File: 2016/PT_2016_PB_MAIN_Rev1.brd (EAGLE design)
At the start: 151.1 x 202.8 mm, 113 parts, among them Q1 Q_IRFS7437PbF, Q11 Q_IRFS7437PbF, Q12 2N7002, Q14 Q_IRFS7437PbF, Q16 Q_IRFS7437PbF, Q20 Q_IRFS7437PbF, Q6 Q_IRFS7437PbF, Q7 Q_IRFS7437PbF, Q9 Q_IRFS7437PbF

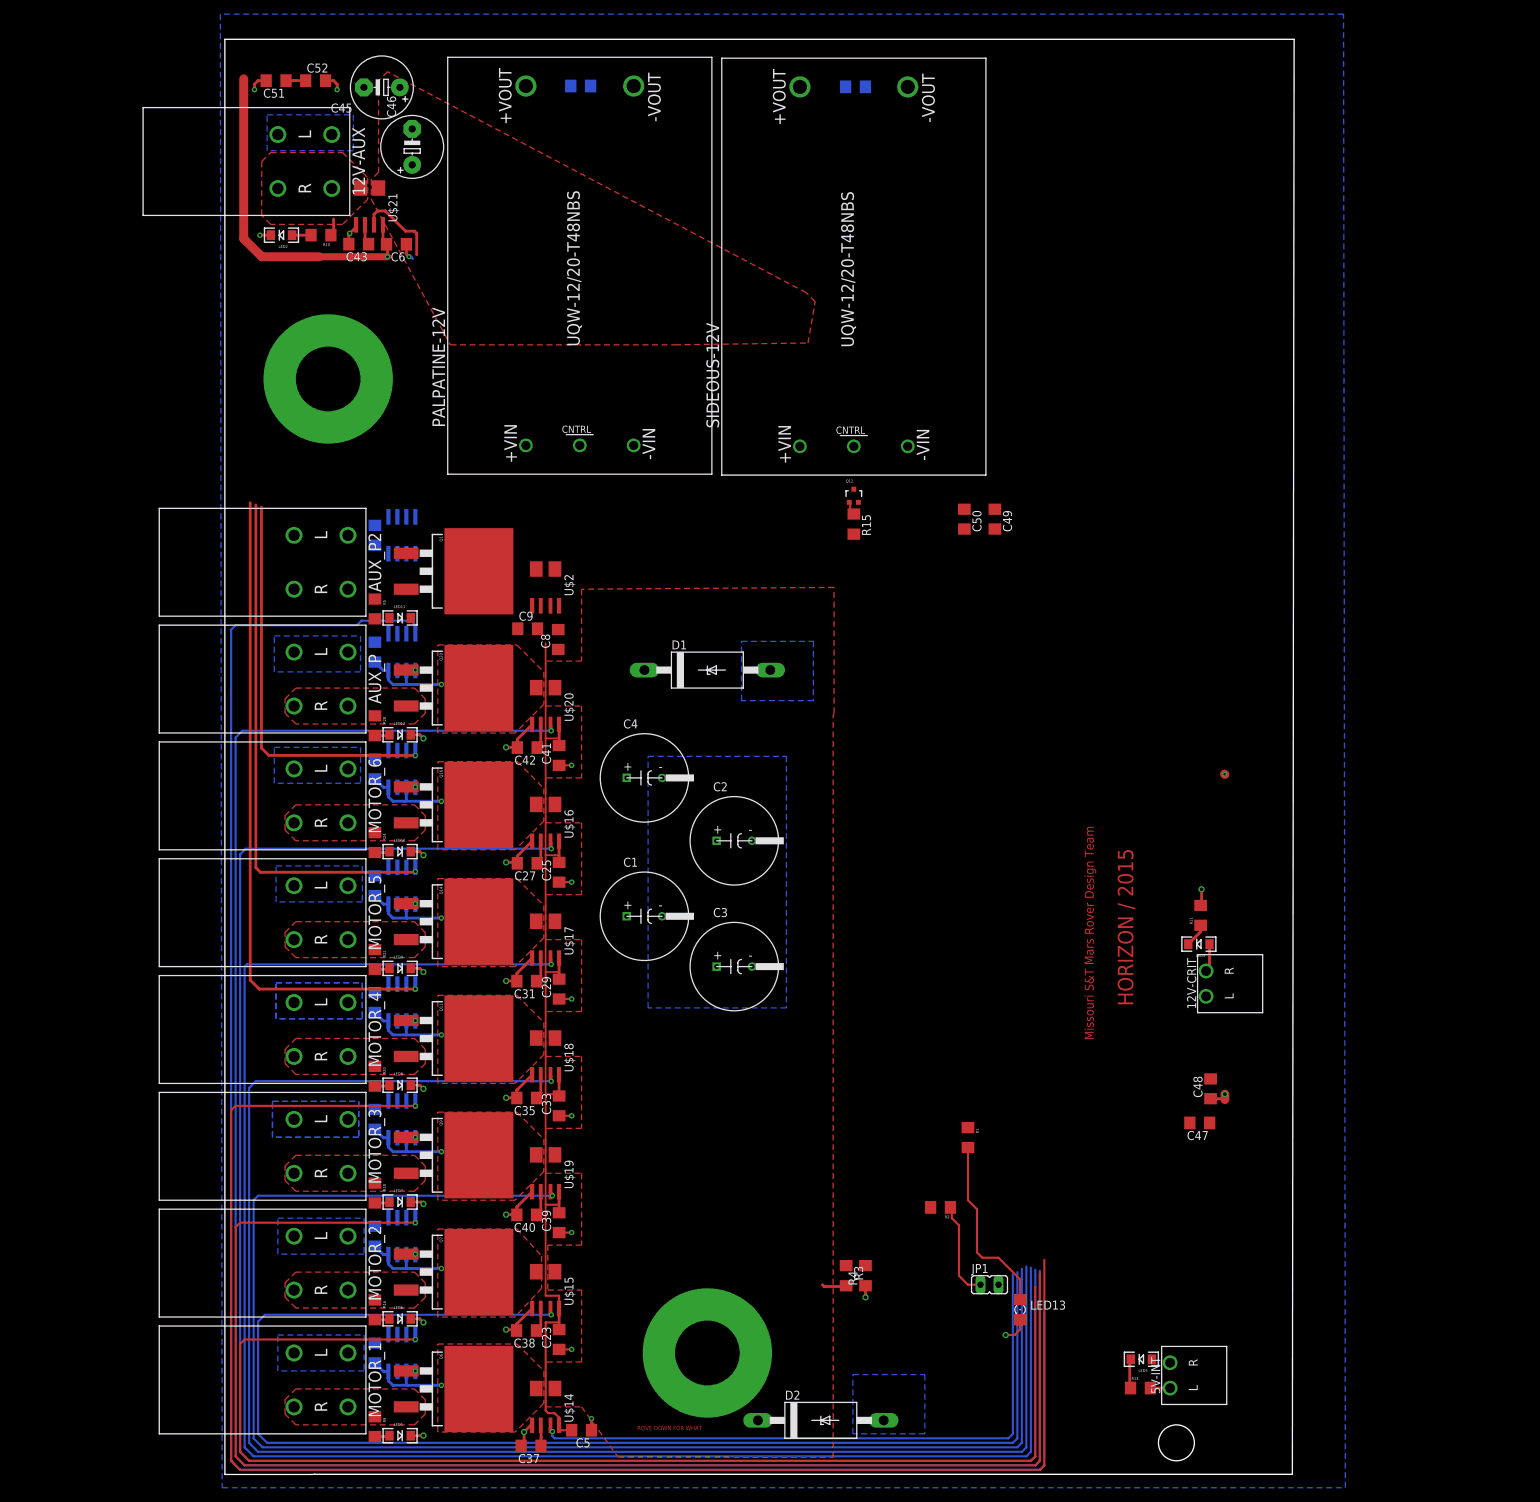
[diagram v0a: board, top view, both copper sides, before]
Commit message: Added Murata 5V Converter and TI uC
Rearranged board
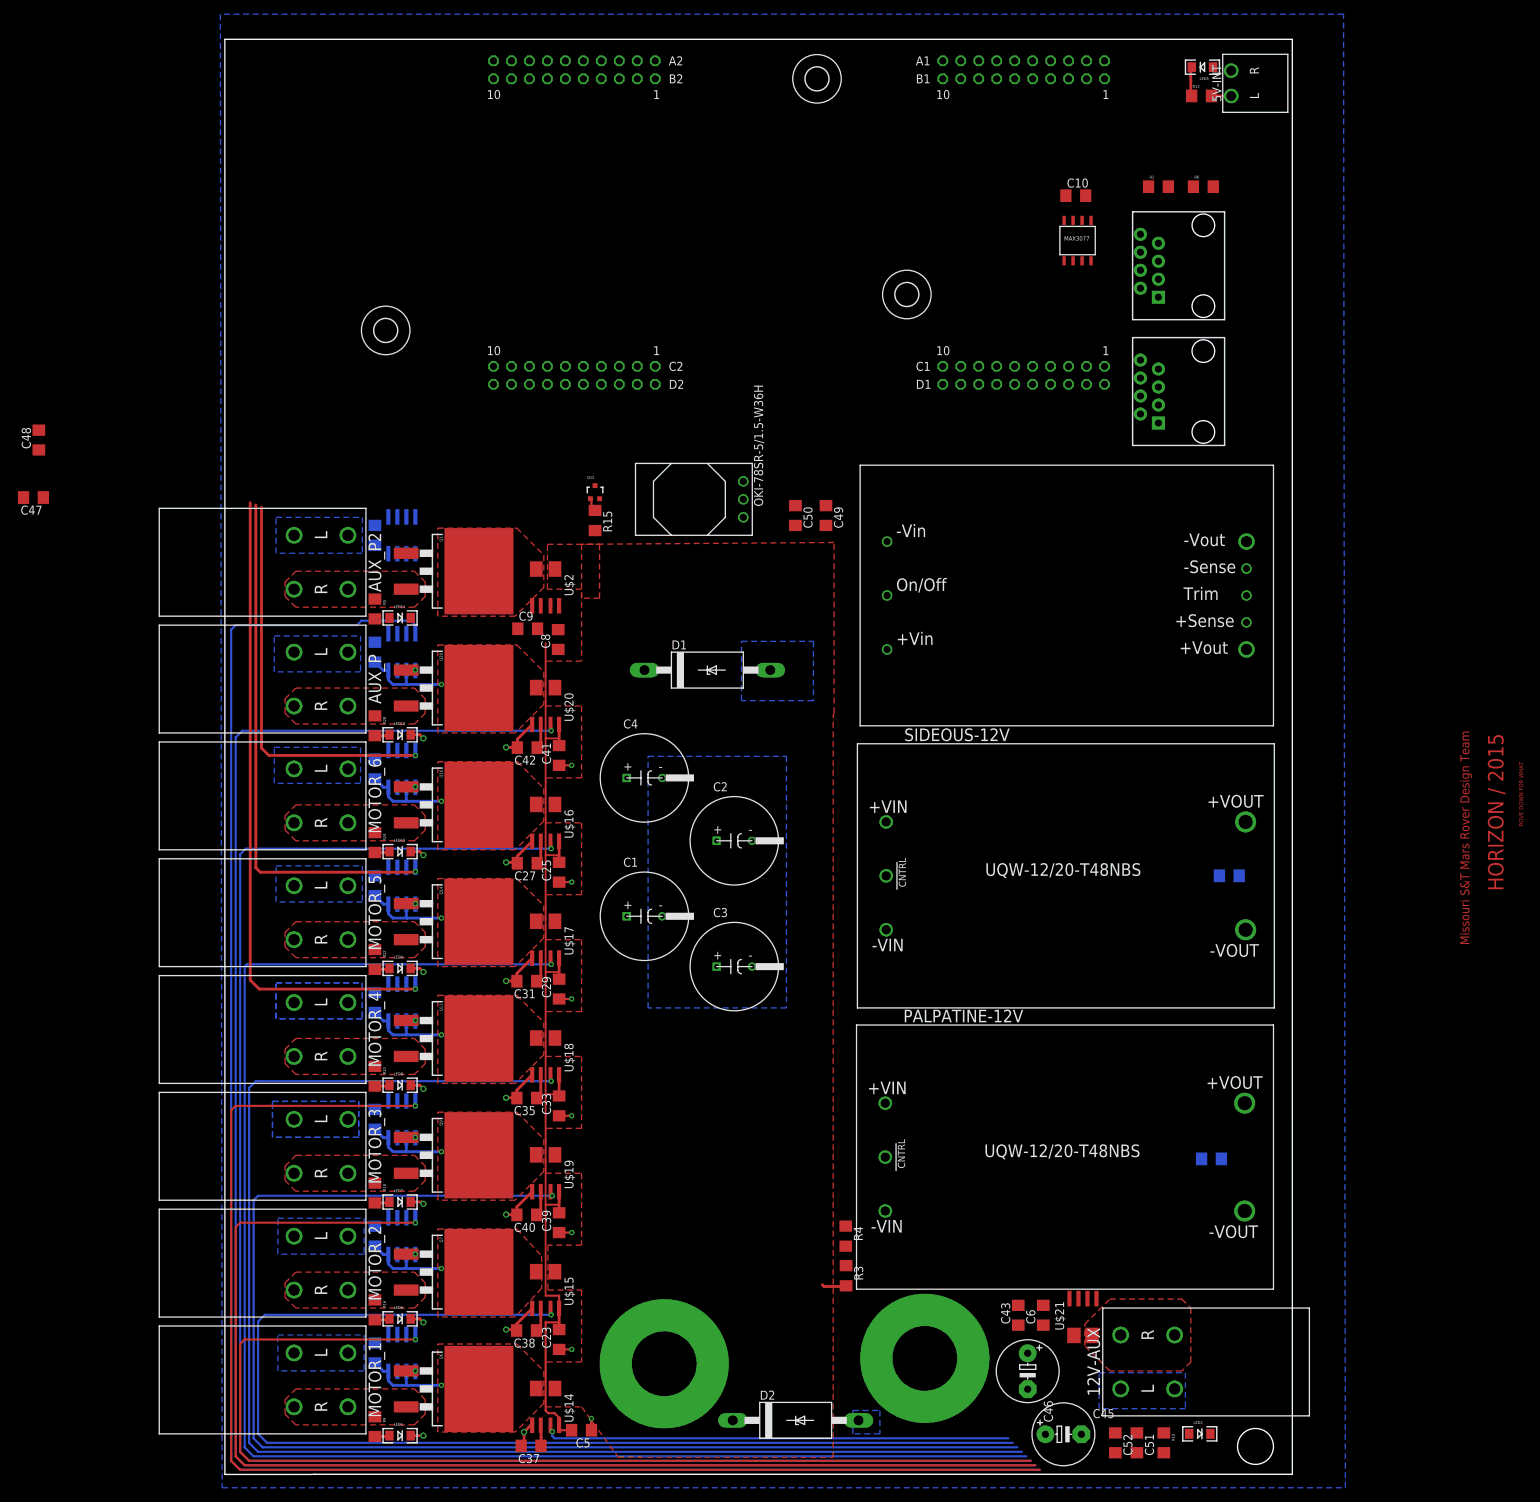
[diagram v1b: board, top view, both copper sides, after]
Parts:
- removed 12V-CRIT: H_WR-TBL_321*0002HORIZ, MRDT-2015-PowerBoard:691322110002
- removed JP1: (no value), jumper:JP1
- removed LED13: (no value), SparkFun-LED:FKIT-LED-1206
- removed LED3: (no value), SparkFun-LED:LED-1206
- removed R11: 1kΩ, SparkFun-Passives:1206
- removed R2: 10k Ohm, SparkFun-Passives:1206
- added C10: 1uF, resistor:C1206
- added OKI-78SR-5/1.5-W36H: Q_OKI-78SR, MRDT-2015-PowerBoard:OKI-78SRH
- added R6: 120 Ohm, SparkFun-Passives:1206
- added U$12: MAX3077, MAX3077:MAX3070E
- added U$23, U$5: RJ45-8PTH, SparkFun-Connectors:RJ45-8
- added U$3: MURATA_5V_DC-DC_CONVERTER, Murata_5V_DC-DC_Converter:MURATA_5V_DC-DC_CONVERTER
- added U$4: TIVA-C-CONNECTED, MRDT-2015-General:TIVA-C-CONNECTED
- R1: value 1k Ohm -> 120 Ohm
- moved C51 227.8 mm to (124.2, 0.00), turned to 270 degrees
- moved C52 223.3 mm to (121.2, 0.00), turned to 270 degrees
- moved LED2 213.4 mm to (133.1, 1.27), turned to 0 degrees
- moved C45 213.4 mm to (113.8, 1.21), turned to 0 degrees
- moved R10 208.1 mm to (128.0, 0.00), turned to 270 degrees
- moved 12V-AUX 207.3 mm to (125.7, 11.4), turned to 90 degrees
- moved C46 193.7 mm to (108.8, 10.1), turned to 270 degrees
- moved C48 189.3 mm to (-31.0, 141.7)
- moved C47 187.0 mm to (-31.8, 133.6)
- moved U$21 186.6 mm to (116.6, 17.8), turned to 0 degrees
- moved 5V-INT 182.8 mm to (137.5, 192.2)
- moved LED5 182.8 mm to (133.5, 194.4)
- moved R13 182.8 mm to (133.3, 190.4)
- moved C43 177.8 mm to (107.4, 18.0), turned to 90 degrees
- moved C6 176.8 mm to (111.0, 18.0), turned to 90 degrees
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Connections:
- removed net 12V-CRIT: 12V-CRIT.R, LED3.A
- removed net INFO_LED: R1.1
- removed net JUMPER_SIG_IN: JP1.1, R2.1
- removed net N$11: LED13.A, R1.2
- new net N$18: R6.1, U$12.Z, U$5.2
- new net N$19: R1.2, U$12.B, U$5.6
- new net N$20: R1.1, U$12.A, U$5.3
- new net N$21: U$12.DI
- new net RXD: U$12.RO
- net +5V: now also C10.1, U$12.VCC; no longer R2.2
- net GND: now also C10.2, U$12.GND, U$5.7, U$5.8; no longer 12V-CRIT.L, JP1.2, LED13.C, R11.2
- net N$3: now also R6.2, U$12.Y, U$5.1; no longer LED3.C, R11.1
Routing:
- net +5V: track 207.1 -> 150.6 mm, vias 3 -> 0
- net M3-SIG: track 221.3 -> 191.3 mm
- net AUX_P-IMEAS: track 288.8 -> 261.1 mm
- net M2-SIG: track 199.7 -> 172.3 mm
- net M6-IMEAS: track 270.3 -> 243.0 mm
- net M5-IMEAS: track 250.3 -> 223.4 mm
- net M4-IMEAS: track 230.4 -> 203.9 mm
- net N$11: track 25.9 -> 0.00 mm
- net M3-IMEAS: track 210.8 -> 185.3 mm
- net M1-SIG: track 178.1 -> 153.3 mm
- net M2-IMEAS: track 190.3 -> 165.9 mm
- net M1-IMEAS: track 89.7 -> 66.2 mm
- net AUX_P-SIG: track 282.8 -> 260.3 mm
- net GND: track 86.8 -> 66.6 mm, vias 29 -> 21
- net JUMPER_SIG_IN: track 13.7 -> 0.00 mm
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- removed copper zone on layer 1, net N$7
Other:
- board size 151.1 x 202.8 mm -> 150.9 x 202.8 mm

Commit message: Added final components and started routing.
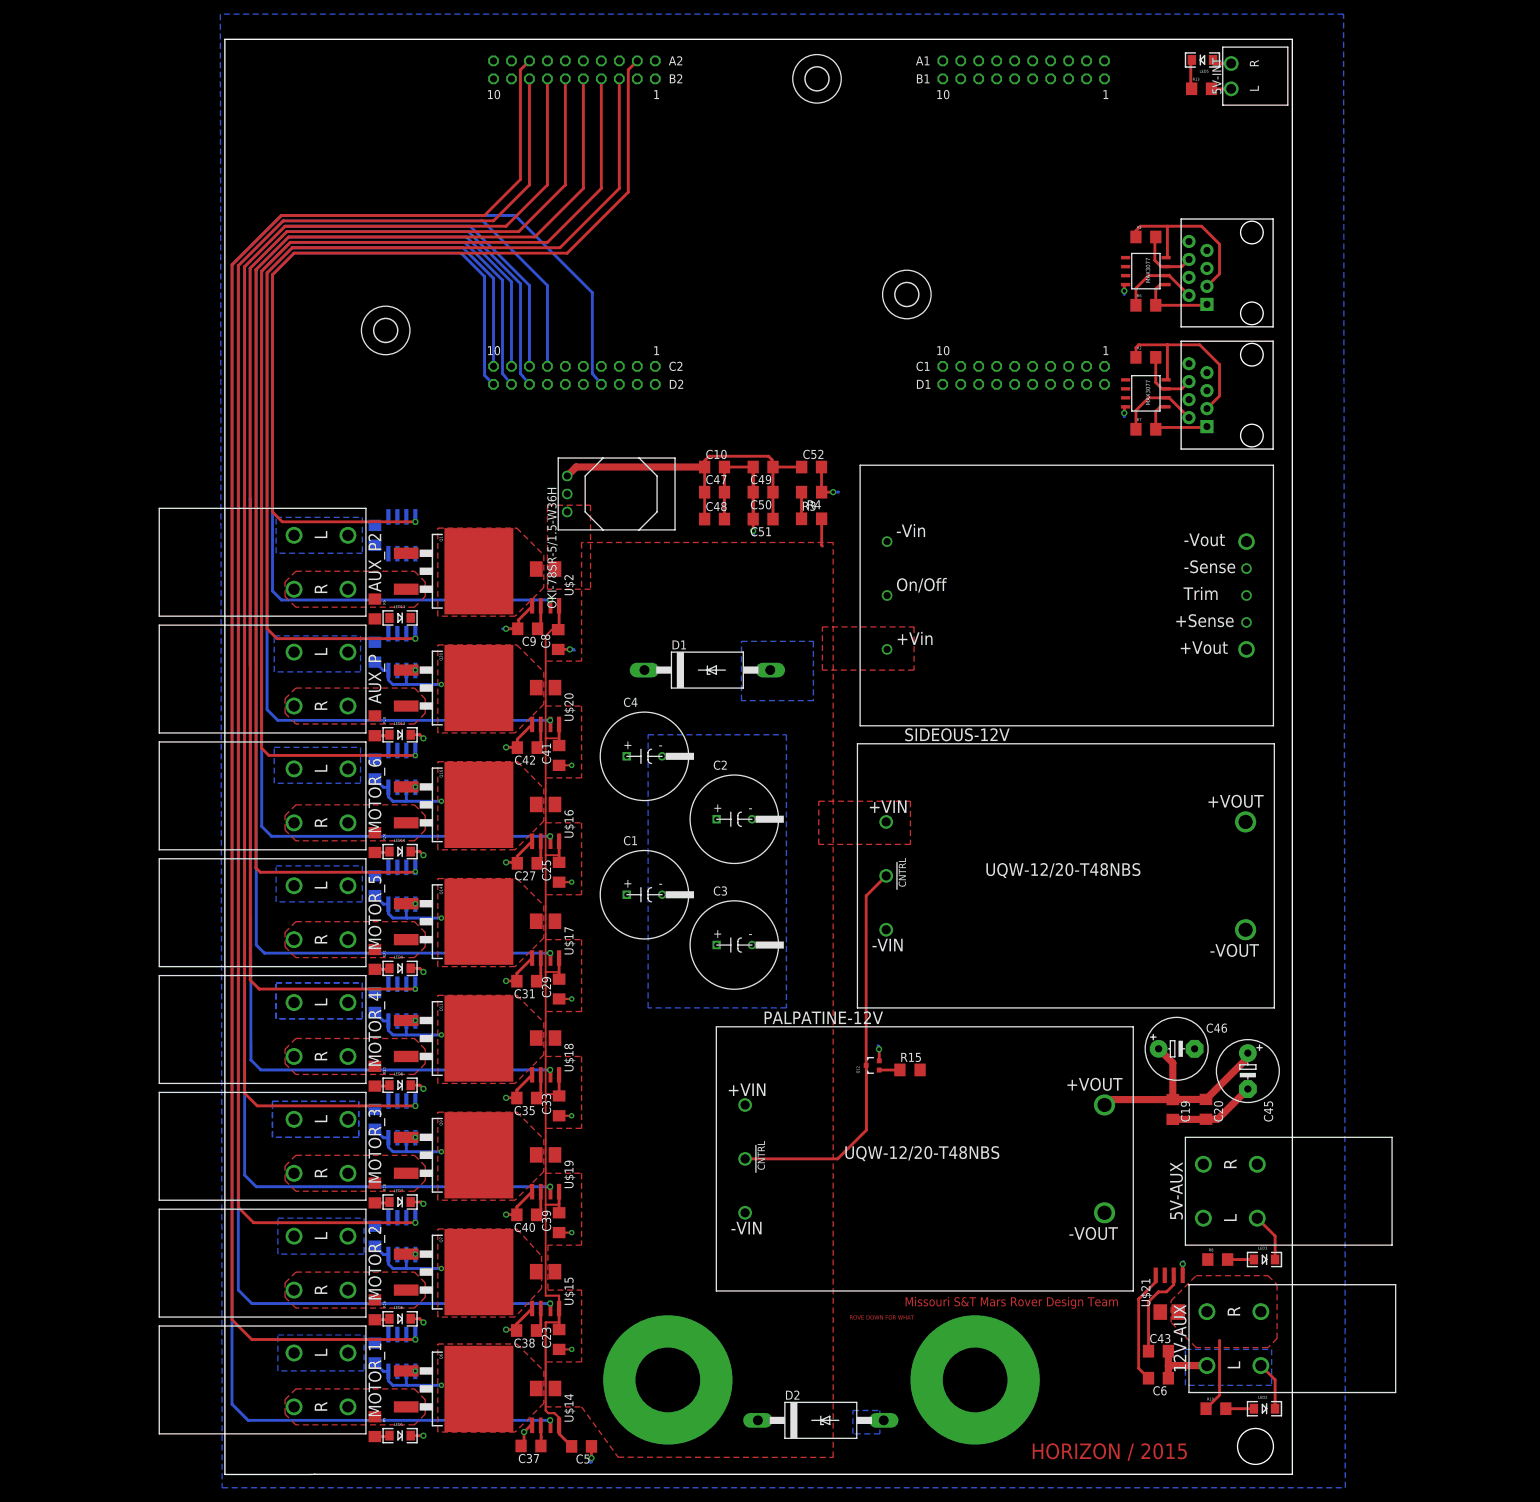
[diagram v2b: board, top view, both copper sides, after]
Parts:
- added 5V-AUX: H_20020618-M02HORIZ, MRDT-2015-PowerBoard:20020618-M02
- added LED3: (no value), SparkFun-LED:LED-1206
- added R2, R7: 120 Ohm, SparkFun-Passives:1206
- added R8: 1kΩ, SparkFun-Passives:1206
- added U$24: MAX3077, MAX3077:MAX3070E
- moved C52 144.4 mm to (78.2, 137.9), turned to 0 degrees
- moved C51 140.8 mm to (71.4, 130.6), turned to 180 degrees
- moved R3 107.1 mm to (78.2, 130.6), turned to 0 degrees
- moved R4 105.3 mm to (78.2, 134.4), turned to 180 degrees
- moved C47 96.3 mm to (64.5, 134.4), turned to 0 degrees
- moved C48 96.2 mm to (64.5, 130.6), turned to 0 degrees
- moved Q12 90.0 mm to (86.9, 53.3), turned to 90 degrees
- moved R15 89.5 mm to (92.1, 52.7), turned to 0 degrees
- moved C10 63.9 mm to (64.5, 137.9)
- moved C45 57.6 mm to (139.9, 52.5), turned to 270 degrees
- moved C46 50.2 mm to (129.8, 55.7), turned to 0 degrees
- moved C20 33.2 mm to (134.0, 47.1), flipped to the top, turned to 270 degrees
- moved OKI-78SR-5/1.5-W36H 24.9 mm to (43.7, 134.1), turned to 270 degrees
- moved C43 20.5 mm to (127.3, 13.0), turned to 0 degrees
- moved PALPATINE-12V 19.8 mm to (94.2, 40.1)
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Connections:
- new net 5V-AUX: 5V-AUX.R1, 5V-AUX.R2, R8.1
- new net 5V_AUX: U$3.P$6
- new net AUX_P2-IMEAS: U$2.7, U$4.PM6
- new net AUX_P2-SIG: U$1.4, U$4.PD2
- new net N$100: U$4.RST1, U$4.RST_2
- new net N$101: U$4.PB2
- new net N$102: U$4.PB3
- new net N$105: U$4.PD0
- new net N$106: U$4.PD1
- new net N$108: U$4.PD3
- new net N$109: U$4.PD4
- new net N$11: R2.2, U$23.6, U$24.B
- new net N$110: U$4.PD5
- new net N$111: U$4.PD7
- new net N$112: U$4.PE0
- new net N$113: U$4.PE1
- new net N$115: U$4.PE2
- new net N$116: U$4.PE3
- new net N$117: U$4.PE4
- new net N$118: U$4.PE5
- new net N$119: U$4.PG0
- new net N$120: U$4.PG1
- new net N$121: U$4.PL0
- new net N$122: U$4.PL1
- new net N$123: U$4.PL2
- new net N$124: U$4.PL3
- new net N$125: U$4.PL4
- new net N$126: U$4.PL5
- new net N$127: U$4.PN2
- new net N$128: U$4.PN3
- new net N$129: U$4.PN4
- new net N$130: U$4.PN5
- new net N$131: U$4.PQ0
- new net N$133: U$4.PQ2/PA3
- new net N$134: U$4.PQ3/PA2
- new net N$32: R2.1, U$23.3, U$24.A
- new net N$33: U$24.DI
- new net N$34: LED3.A, R8.2
- new net N$35: U$4.PA4
- new net N$36: U$4.PA5
- new net N$37: U$4.PA6
- new net N$43: U$4.PC4
- new net N$48: U$4.PC5
- new net N$5: R7.2, U$23.1, U$24.Y
- new net N$50: U$4.PC6
- new net N$51: U$4.PC7
- new net N$52: U$4.PF1
- new net N$53: U$4.PF2
- new net N$58: U$4.PF3
- new net N$65: U$4.PH2
- new net N$70: U$4.PH3
- new net N$75: U$4.PK4
- new net N$76: U$4.PK5
- new net N$8: R7.1, U$23.2, U$24.Z
- new net N$83: U$4.PM0
- new net N$84: U$4.PM1
- new net N$85: U$4.PM2
- new net N$86: U$4.PM3
- new net N$87: U$4.PM4
- new net N$88: U$4.PM5
- new net N$90: U$4.PM7
- new net N$91: U$4.PP0
- new net N$92: U$4.PP1
- new net N$93: U$4.PP2
- new net N$97: U$4.+5V_1, U$4.+5V_2
- new net N$98: U$4.+3V3_1, U$4.+3V3_2
- new net N$99: U$4.GND_1, U$4.GND_2, U$4.GND_3, U$4.GND_4
- new net RXD1: U$24.RO
- net +5V: now also OKI-78SR-5/1.5-W36H.3, U$24.VCC
- net AUX_P-IMEAS: now also U$4.PK7; no longer U$2.7
- net AUX_P-SIG: now also U$4.PB4; no longer U$1.4
- net GND: now also 5V-AUX.L1, 5V-AUX.L2, LED3.C, OKI-78SR-5/1.5-W36H.2, U$23.7, U$23.8, U$24.GND, U$3.P$2, U$3.P$5
- net M1-IMEAS: now also U$4.PA7
- net M1-SIG: now also U$4.PP4
- net M2-IMEAS: now also U$4.PH0
- net M2-SIG: now also U$4.PK3
- net M3-IMEAS: now also U$4.PH1
- net M3-SIG: now also U$4.PK2
- net M4-IMEAS: now also U$4.PP3
- net M4-SIG: now also U$4.PK1
- net M5-IMEAS: now also U$4.PK6
- net M5-SIG: now also U$4.PK0
- net M6-IMEAS: now also U$4.PQ1
- net M6-SIG: now also U$4.PB5
- net V_BATT: now also OKI-78SR-5/1.5-W36H.1, U$3.P$3
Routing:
- net M1-IMEAS: track 66.2 -> 279.4 mm
- net AUX_P2-IMEAS: track 0.00 -> 133.7 mm, vias 0 -> 1
- net AUX_P2-SIG: track 0.00 -> 129.2 mm, vias 0 -> 1
- net AUX_P-SIG: track 260.3 -> 142.7 mm, vias 0 -> 1
- net AUX_P-IMEAS: track 261.1 -> 150.7 mm
- net M6-SIG: track 56.9 -> 158.6 mm
- net M5-SIG: track 74.8 -> 174.6 mm
- net M4-SIG: track 92.0 -> 189.6 mm
- net M1-SIG: track 153.3 -> 239.9 mm
- net GND: track 66.6 -> 153.0 mm, vias 21 -> 29
- net M2-IMEAS: track 165.9 -> 251.9 mm
- net +5V: track 150.6 -> 228.2 mm
- net M6-IMEAS: track 243.0 -> 174.6 mm
- net N$4: track 0.00 -> 56.0 mm
- net M2-SIG: track 172.3 -> 220.6 mm
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- added copper zone on layer 1, net N$10
- added copper zone on layer 1, net N$9
